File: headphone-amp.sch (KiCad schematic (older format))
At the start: 27 parts, among them J1 AudioJack4, J2 AudioJack4, J3 Conn_01x02_Male, SW1 SW_SPDT, U1 RC4580, U2 TMA0512D

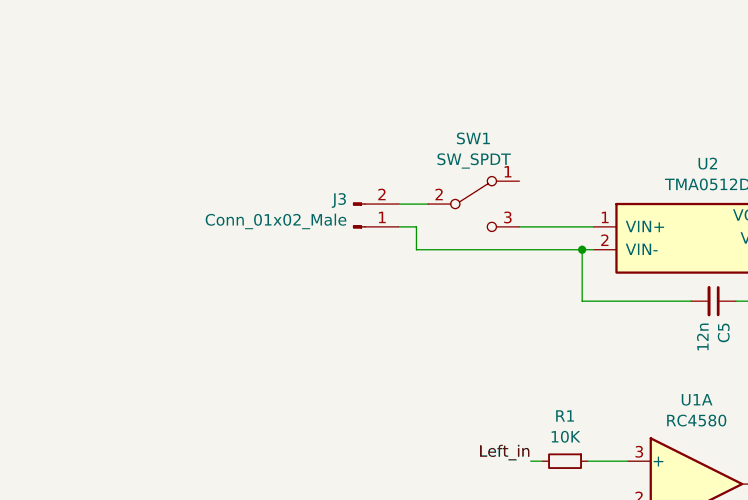
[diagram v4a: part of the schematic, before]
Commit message: added input filtering to DC-DC converter
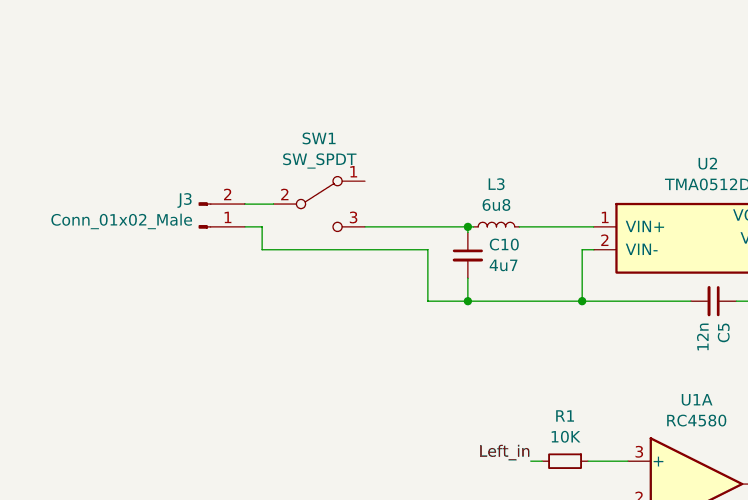
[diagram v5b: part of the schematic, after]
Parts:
- added C10: 4u7, Capacitor_SMD:C_0805_2012Metric, symbol Device:C_Small
- added L3: 6u8, Inductor_SMD:L_0805_2012Metric, symbol Device:L_Small
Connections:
- net at SW1.3 (C): now also C10.1, L3.1; no longer U2.1 (VIN+)
- net at C5.2, J3.1 (Pin_1), U2.2 (VIN-): now also C10.2
- new net: L3.2, U2.1 (VIN+)
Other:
- moved on the sheet: J3, SW1
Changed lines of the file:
@@
 L Connector:Conn_01x02_Male J3
 U 1 1 5C5AEB8B
-P 2600 2150
-F 0 "J3" H 2572 2030 50  0000 R CNN
-F 1 "Conn_01x02_Male" H 2572 2121 50  0000 R CNN
-F 2 "Connector_JST:JST_PH_S2B-PH-SM4-TB_1x02-1MP_P2.00mm_Horizontal" H 2600 2150 50  0001 C CNN
-F 3 "~" H 2600 2150 50  0001 C CNN
-	1    2600 2150
+P 1925 2150
+F 0 "J3" H 1897 2030 50  0000 R CNN
+F 1 "Conn_01x02_Male" H 1897 2121 50  0000 R CNN
+F 2 "Connector_JST:JST_PH_S2B-PH-SM4-TB_1x02-1MP_P2.00mm_Horizontal" H 1925 2150 50  0001 C CNN
+F 3 "~" H 1925 2150 50  0001 C CNN
+	1    1925 2150
 	1    0    0    1
 $EndComp
@@
 L Switch:SW_SPDT SW1
 U 1 1 5C59CAE8
-P 3125 2050
-F 0 "SW1" H 3125 2335 50  0000 C CNN
-F 1 "SW_SPDT" H 3125 2244 50  0000 C CNN
-F 2 "Button_Switch_SMD:SW_SPDT_CK-JS102011SAQN" H 3125 2050 50  0001 C CNN
-F 3 "" H 3125 2050 50  0001 C CNN
-	1    3125 2050
-	1    0    0    -1
-$EndComp
-Wire Wire Line
-	2925 2050 2800 2050
-Wire Wire Line
-	2800 2150 2875 2150
-Wire Wire Line
-	2875 2150 2875 2250
+P 2450 2050
+F 0 "SW1" H 2450 2335 50  0000 C CNN
+F 1 "SW_SPDT" H 2450 2244 50  0000 C CNN
+F 2 "Button_Switch_SMD:SW_SPDT_CK-JS102011SAQN" H 2450 2050 50  0001 C CNN
+F 3 "" H 2450 2050 50  0001 C CNN
+	1    2450 2050
+	1    0    0    -1
+$EndComp
+Wire Wire Line
+	2250 2050 2125 2050
+Wire Wire Line
+	2125 2150 2200 2150
+Wire Wire Line
+	2200 2150 2200 2250
 Wire Wire Line
 	3325 2150 3650 2150
 Wire Wire Line
-	2875 2250 3600 2250
+	2200 2250 2925 2250
 $Comp
 L Device:C_Small C5
@@
 Wire Wire Line
 	3600 2475 3600 2250
-Connection ~ 3600 2250
 Wire Wire Line
 	3600 2250 3650 2250
@@
 Text Notes 5050 2600 0    50   ~ 0
 20u = 2x stacked 10u
+$Comp
+L Device:L_Small L3
+U 1 1 5C6385B7
+P 3225 2150
+F 0 "L3" V 3410 2150 50  0000 C CNN
+F 1 "6u8" V 3319 2150 50  0000 C CNN
+F 2 "Inductor_SMD:L_0805_2012Metric" H 3225 2150 50  0001 C CNN
+F 3 "~" H 3225 2150 50  0001 C CNN
+	1    3225 2150
+	0    -1   -1   0
+$EndComp
+$Comp
+L Device:C_Small C10
+U 1 1 5C638703
+P 3100 2275
+F 0 "C10" H 3192 2321 50  0000 L CNN
+F 1 "4u7" H 3192 2230 50  0000 L CNN
+F 2 "Capacitor_SMD:C_0805_2012Metric" H 3100 2275 50  0001 C CNN
+F 3 "~" H 3100 2275 50  0001 C CNN
+	1    3100 2275
+	1    0    0    -1
+$EndComp
+Wire Wire Line
+	3125 2150 3100 2150
+Wire Wire Line
+	3100 2150 3100 2175
+Wire Wire Line
+	3100 2150 2650 2150
+Connection ~ 3100 2150
+Wire Wire Line
+	2925 2250 2925 2475
+Wire Wire Line
+	2925 2475 3100 2475
+Connection ~ 3600 2475
+Wire Wire Line
+	3100 2375 3100 2475
+Connection ~ 3100 2475
+Wire Wire Line
+	3100 2475 3600 2475
 $EndSCHEMATC

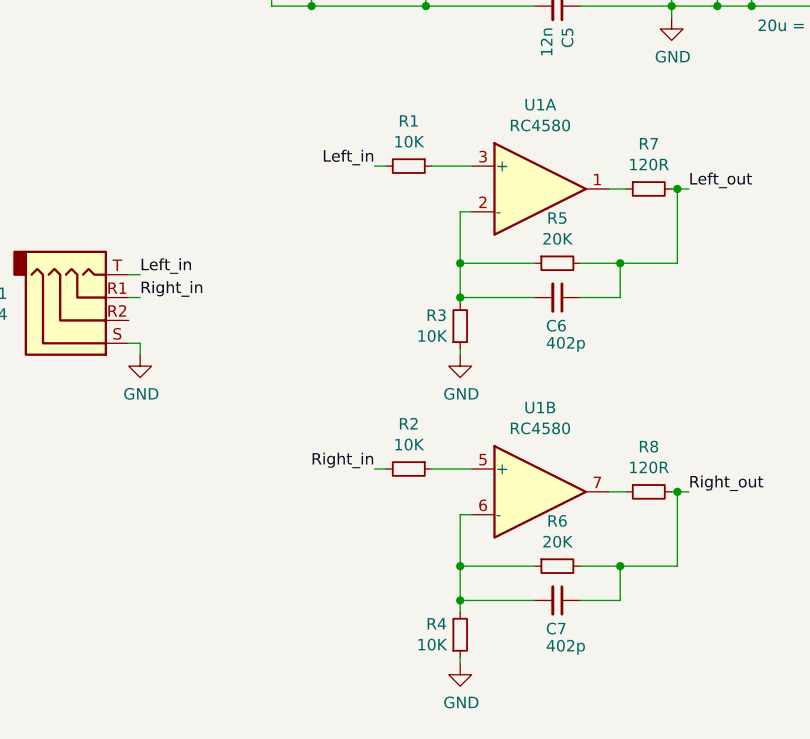
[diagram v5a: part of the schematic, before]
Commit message: Added input resistors
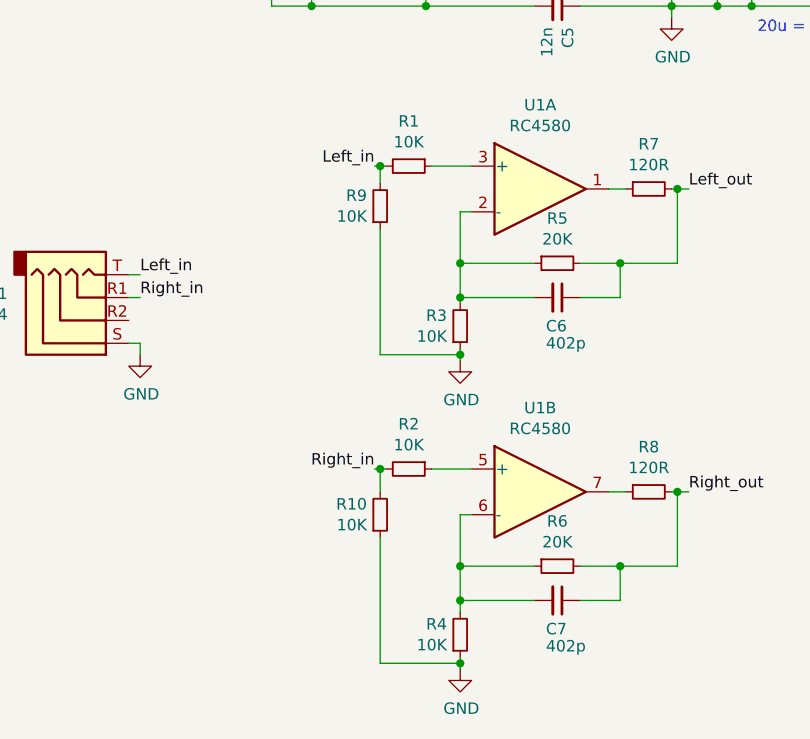
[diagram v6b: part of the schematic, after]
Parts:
- added R10, R9: 10K, Resistor_SMD:R_0805_2012Metric, symbol Device:R_Small
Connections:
- net GND: now also R10.1, R9.1
- net Left_in: now also R9.2
- net Right_in: now also R10.2
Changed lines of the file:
@@
 Left_in
 Wire Wire Line
-	3375 3175 3425 3175
+	3375 3175 3400 3175
 $Comp
 L power:GND #PWR0102
 U 1 1 5C5A651D
-P 3750 4000
-F 0 "#PWR0102" H 3750 3750 50  0001 C CNN
-F 1 "GND" H 3755 3827 50  0000 C CNN
-F 2 "" H 3750 4000 50  0001 C CNN
-F 3 "" H 3750 4000 50  0001 C CNN
-	1    3750 4000
-	1    0    0    -1
-$EndComp
-Wire Wire Line
-	3750 4000 3750 3975
+P 3750 4025
+F 0 "#PWR0102" H 3750 3775 50  0001 C CNN
+F 1 "GND" H 3755 3852 50  0000 C CNN
+F 2 "" H 3750 4025 50  0001 C CNN
+F 3 "" H 3750 4025 50  0001 C CNN
+	1    3750 4025
+	1    0    0    -1
+$EndComp
+Wire Wire Line
+	3750 4025 3750 4000
 Text Label 4750 3275 0    50   ~ 0
 Left_out
@@
 Right_in
 Wire Wire Line
-	3375 4500 3425 4500
+	3375 4500 3400 4500
 $Comp
 L power:GND #PWR0108
 U 1 1 5C5AADC9
-P 3750 5350
-F 0 "#PWR0108" H 3750 5100 50  0001 C CNN
-F 1 "GND" H 3755 5177 50  0000 C CNN
-F 2 "" H 3750 5350 50  0001 C CNN
-F 3 "" H 3750 5350 50  0001 C CNN
-	1    3750 5350
-	1    0    0    -1
-$EndComp
-Wire Wire Line
-	3750 5350 3750 5325
+P 3750 5375
+F 0 "#PWR0108" H 3750 5125 50  0001 C CNN
+F 1 "GND" H 3755 5202 50  0000 C CNN
+F 2 "" H 3750 5375 50  0001 C CNN
+F 3 "" H 3750 5375 50  0001 C CNN
+	1    3750 5375
+	1    0    0    -1
+$EndComp
+Wire Wire Line
+	3750 5375 3750 5350
 Text Label 4750 4600 0    50   ~ 0
 Right_out
@@
 Wire Wire Line
 	3100 2475 3600 2475
+$Comp
+L Device:R_Small R9
+U 1 1 5C64700C
+P 3400 3350
+F 0 "R9" H 3342 3304 50  0000 R CNN
+F 1 "10K" H 3342 3395 50  0000 R CNN
+F 2 "Resistor_SMD:R_0805_2012Metric" H 3400 3350 50  0001 C CNN
+F 3 "~" H 3400 3350 50  0001 C CNN
+	1    3400 3350
+	1    0    0    1
+$EndComp
+Wire Wire Line
+	3400 3250 3400 3175
+Connection ~ 3400 3175
+Wire Wire Line
+	3400 3175 3425 3175
+Wire Wire Line
+	3750 4000 3400 4000
+Wire Wire Line
+	3400 4000 3400 3450
+Connection ~ 3750 4000
+Wire Wire Line
+	3750 4000 3750 3975
+$Comp
+L Device:R_Small R10
+U 1 1 5C6549E8
+P 3400 4700
+F 0 "R10" H 3342 4654 50  0000 R CNN
+F 1 "10K" H 3342 4745 50  0000 R CNN
+F 2 "Resistor_SMD:R_0805_2012Metric" H 3400 4700 50  0001 C CNN
+F 3 "~" H 3400 4700 50  0001 C CNN
+	1    3400 4700
+	1    0    0    1
+$EndComp
+Wire Wire Line
+	3400 4500 3400 4600
+Connection ~ 3400 4500
+Wire Wire Line
+	3400 4500 3425 4500
+Wire Wire Line
+	3400 4800 3400 5350
+Wire Wire Line
+	3400 5350 3750 5350
+Connection ~ 3750 5350
+Wire Wire Line
+	3750 5350 3750 5325
 $EndSCHEMATC
